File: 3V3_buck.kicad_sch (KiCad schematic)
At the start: 14 parts, among them U7 LV14540DDAR

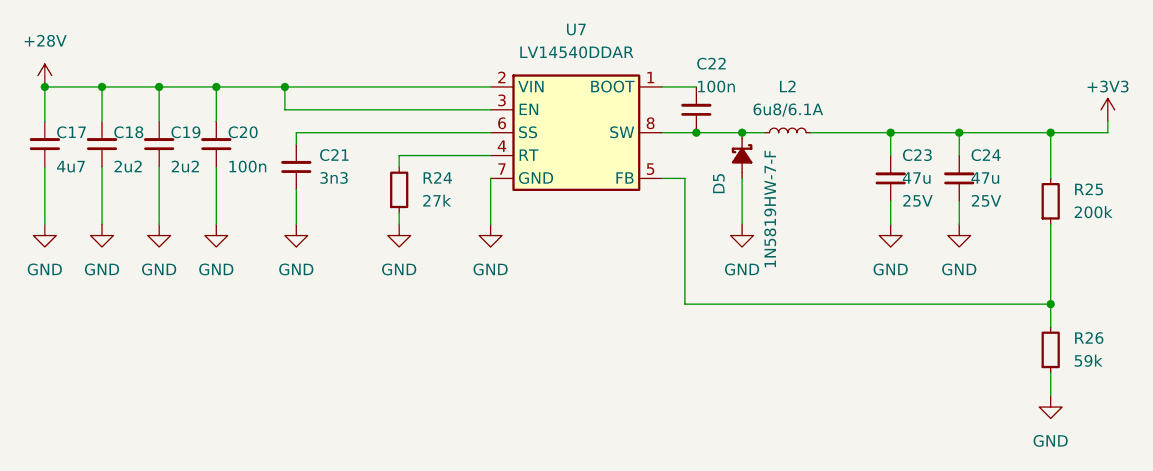
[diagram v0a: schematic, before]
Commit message: [#62623] Improve schematic, change 3V3 buck inductor, correct SPI, add testpoint
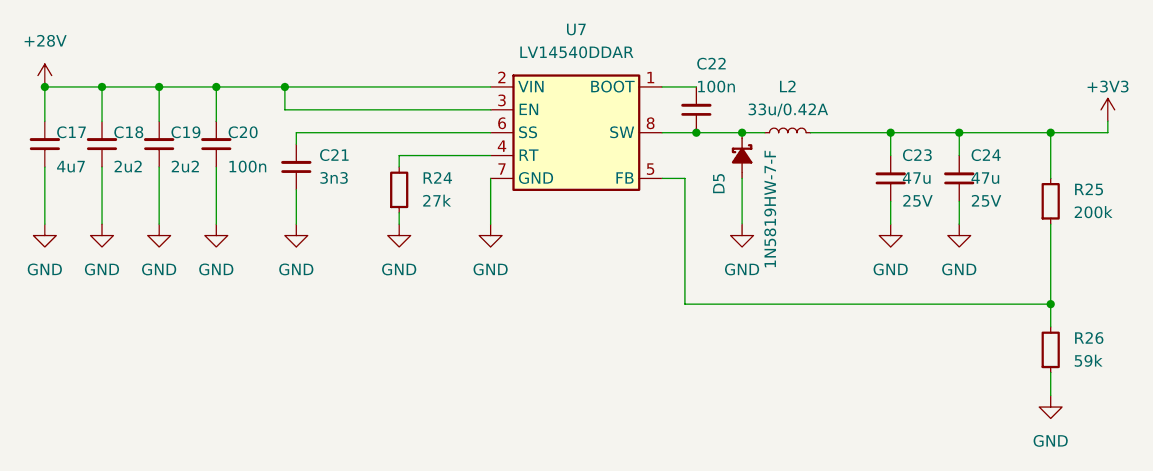
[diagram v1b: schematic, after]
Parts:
- removed L2: L_6u8_6.1A_MPS-MPL-AL5050, antmicro-footprints:L_MPS-MPL-AL5050, symbol antmicroFixedInductors:L_6u8_6.1A_MPS-MPL-AL5050
- added L2: L_33u_0.42A_WE-TPC-3816, antmicro-footprints:L_WE-TPC-3816, symbol antmicroFixedInductors:L_33u_0.42A_WE-TPC-3816
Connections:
- net +3V3: now also L2.2
- net at C22.1, D5.1 (C), U7.8 (SW): now also L2.1
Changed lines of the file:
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@@
+    )
+  )
+  (symbol (lib_id "antmicroFixedInductors:L_33u_0.42A_WE-TPC-3816") (at 168.91 85.09 0) (unit 1)
+    (in_bom yes) (on_board yes) (dnp no) (fields_autoplaced)
+    (property "Reference" "L2" (at 171.45 80.01 0)
+      (effects (font (size 1.27 1.27) (thickness 0.15)))
+    )
+    (property "Value" "L_33u_0.42A_WE-TPC-3816" (at 182.88 87.63 0)
+      (effects (font (size 1.27 1.27) (thickness 0.15)) (justify left bottom) hide)
+    )
+    (property "Footprint" "antmicro-footprints:L_WE-TPC-3816" (at 182.88 92.71 0)
+      (effects (font (size 1.27 1.27) (thickness 0.15)) (justify left bottom) hide)
+    )
+    (property "Datasheet" "https://www.we-online.com/components/products/datasheet/744031330.pdf" (at 182.88 95.25 0)
+      (effects (font (size 1.27 1.27) (thickness 0.15)) (justify left bottom) hide)
+    )
+    (property "Val" "33u/0.42A" (at 171.45 82.55 0)
+      (effects (font (size 1.27 1.27) (thickness 0.15)))
+    )
+    (property "Manufacturer" "Würth Elektronik" (at 182.88 97.79 0)
+      (effects (font (size 1.27 1.27) (thickness 0.15)) (justify left bottom) hide)
+    )
+    (property "MPN" "744031330" (at 182.88 100.33 0)
+      (effects (font (size 1.27 1.27) (thickness 0.15)) (justify left bottom) hide)
+    )
+    (property "ISat" "0.32 A" (at 182.88 101.6 0)
+      (effects (font (size 1.27 1.27)) (justify left) hide)
+    )
+    (property "IMax" "0.42 A" (at 182.88 105.41 0)
+      (effects (font (size 1.27 1.27) (thickness 0.15)) (justify left bottom) hide)
+    )
+    (property "Size" "3.8x3.8" (at 182.88 107.95 0)
+      (effects (font (size 1.27 1.27) (thickness 0.15)) (justify left bottom) hide)
+    )
+    (property "Author" "Antmicro" (at 182.88 110.49 0)
+      (effects (font (size 1.27 1.27) (thickness 0.15)) (justify left bottom) hide)
+    )
+    (property "License" "Apache-2.0" (at 182.88 113.03 0)
+      (effects (font (size 1.27 1.27) (thickness 0.15)) (justify left bottom) hide)
+    )
+    (pin "2")
+    (pin "1")
+    (instances
+      (project "antmicro-poe-to-usbc-pd-adapter"
+        (path "/cf0d4429-3f03-449f-96a7-26d69371a46d/b0b823e2-9d24-4e97-9cf1-ee0d4770eeee"
+          (reference "L2") (unit 1)
+        )
+      )
     )
   )
@@
         )
       )
-    )
-  )
-  (symbol (lib_id "antmicroFixedInductors:L_6u8_6.1A_MPS-MPL-AL5050") (at 168.91 85.09 0) (unit 1)
-    (in_bom yes) (on_board yes) (dnp no) (fields_autoplaced)
-    (property "Reference" "L2" (at 171.45 80.01 0)
-      (effects (font (size 1.27 1.27) (thickness 0.15)))
-    )
-    (property "Value" "L_6u8_6.1A_MPS-MPL-AL5050" (at 182.88 87.63 0)
-      (effects (font (size 1.27 1.27) (thickness 0.15)) (justify left bottom) hide)
-    )
-    (property "Footprint" "antmicro-footprints:L_MPS-MPL-AL5050" (at 182.88 92.71 0)
-      (effects (font (size 1.27 1.27) (thickness 0.15)) (justify left bottom) hide)
-    )
-    (property "Datasheet" "https://www.monolithicpower.com/en/documentview/productdocument/index/version/2/document_type/Datasheet/lang/en/sku/MPL-AL5050-6R8/document_id/5811/" (at 182.88 95.25 0)
-      (effects (font (size 1.27 1.27) (thickness 0.15)) (justify left bottom) hide)
-    )
-    (property "Val" "6u8/6.1A" (at 171.45 82.55 0)
-      (effects (font (size 1.27 1.27) (thickness 0.15)))
-    )
-    (property "Manufacturer" "Monolithic Power Systems" (at 182.88 97.79 0)
-      (effects (font (size 1.27 1.27) (thickness 0.15)) (justify left bottom) hide)
-    )
-    (property "MPN" "MPL-AL5050-6R8" (at 182.88 100.33 0)
-      (effects (font (size 1.27 1.27) (thickness 0.15)) (justify left bottom) hide)
-    )
-    (property "ISat" "7.6 A" (at 182.88 101.6 0)
-      (effects (font (size 1.27 1.27)) (justify left) hide)
-    )
-    (property "IMax" "6.1 A" (at 182.88 105.41 0)
-      (effects (font (size 1.27 1.27) (thickness 0.15)) (justify left bottom) hide)
-    )
-    (property "Size" "5.5x5.3" (at 182.88 107.95 0)
-      (effects (font (size 1.27 1.27) (thickness 0.15)) (justify left bottom) hide)
-    )
-    (property "Author" "Antmicro" (at 182.88 110.49 0)
-      (effects (font (size 1.27 1.27) (thickness 0.15)) (justify left bottom) hide)
-    )
-    (property "License" "Apache-2.0" (at 182.88 113.03 0)
-      (effects (font (size 1.27 1.27) (thickness 0.15)) (justify left bottom) hide)
-    )
-    (pin "2")
-    (pin "1")
-    (instances
-      (project "antmicro-poe-to-usbc-pd-adapter"
-        (path "/cf0d4429-3f03-449f-96a7-26d69371a46d/b0b823e2-9d24-4e97-9cf1-ee0d4770eeee"
-          (reference "L2") (unit 1)
-        )
-      )
